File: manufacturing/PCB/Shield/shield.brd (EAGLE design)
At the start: 95 x 85 mm, 230 parts, among them J1 DC_JACK, Q1 12 MHz, T1 PHKD3NQ10T, U1 UCC27531, U10 UCC27531, U11 UCC27531, U12 UCC27531, U13 UCC27531, U14 UCC27531, U15 UCC27531, U16 UCC27531, U17 UCC27531, U18 UCC27531, U19 UCC27531, U2 UCC27531, U20 UCC27531, U21 UCC27531, U22 UCC27531, U23 UCC27531, U24 UCC27531, U25 UCC27531, U26 UCC27531, U27 UCC27531, U28 UCC27531, U29 UCC27531, U3 UCC27531, U30 UCC27531, U31 UCC27531, U32 UCC27531, U33 UCC27531, U34 UCC27531, U35 UCC27531, U36 UCC27531, U37 UCC27531, U38 UCC27531, U39 UCC27531, U4 UCC27531, U40 UCC27531, U41 UCC27531, U42 UCC27531, U43 UCC27531, U44 UCC27531, U45 UCC27531, U46 UCC27531, U47 UCC27531, U48 UCC27531, U49 UCC27531, U5 UCC27531, U50 UCC27531, U51 UCC27531, U52 UCC27531, U53 UCC27531, U54 UCC27531, U55 UCC27531, U56 UCC27531, U57 UCC27531, U58 UCC27531, U59 UCC27531, U6 UCC27531, U60 UCC27531, U61 UCC27531, U62 UCC27531, U63 UCC27531, U64 UCC27531, U65 LTC4365, U66 FT232R, U7 UCC27531, U8 UCC27531, U9 UCC27531, X1 MINI-USB, X2 BNC

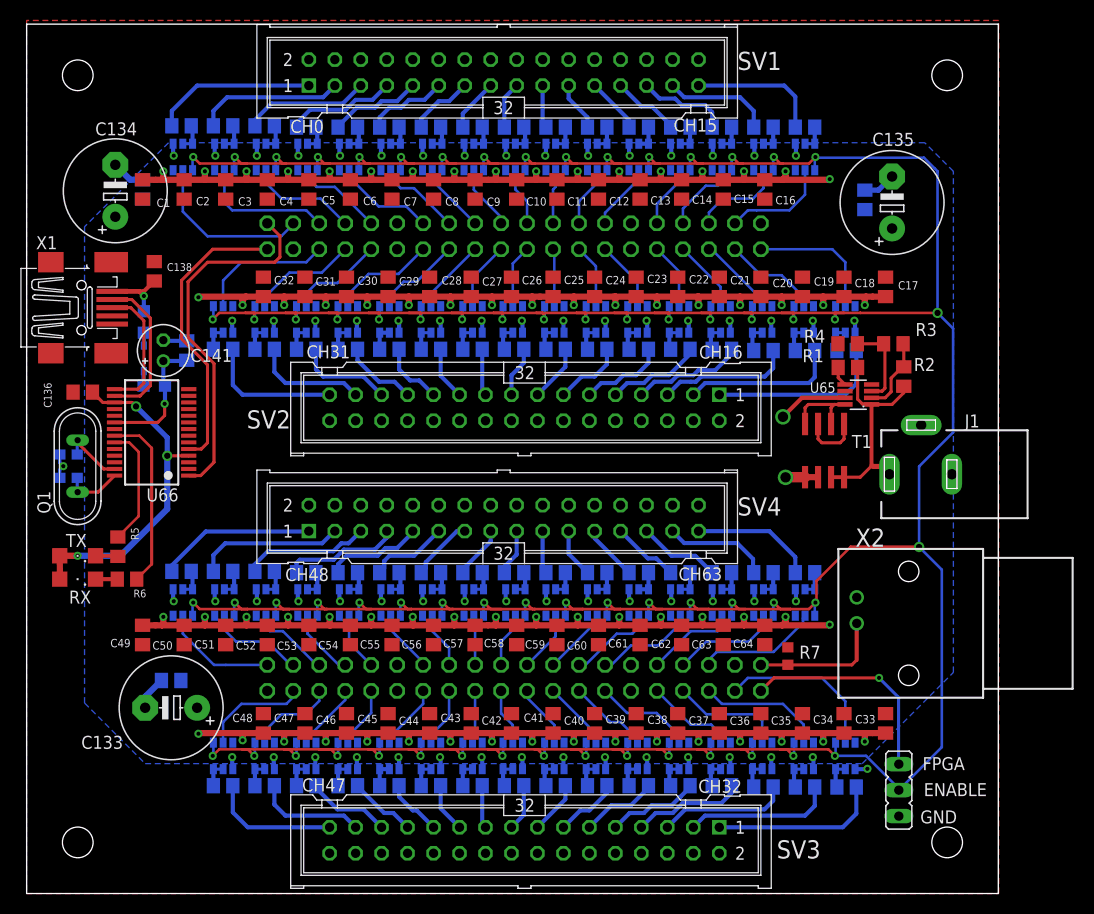
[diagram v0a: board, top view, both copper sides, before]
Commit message: fixed RX/TX swap, added power from USB option (Shield v1.1 ready for production)
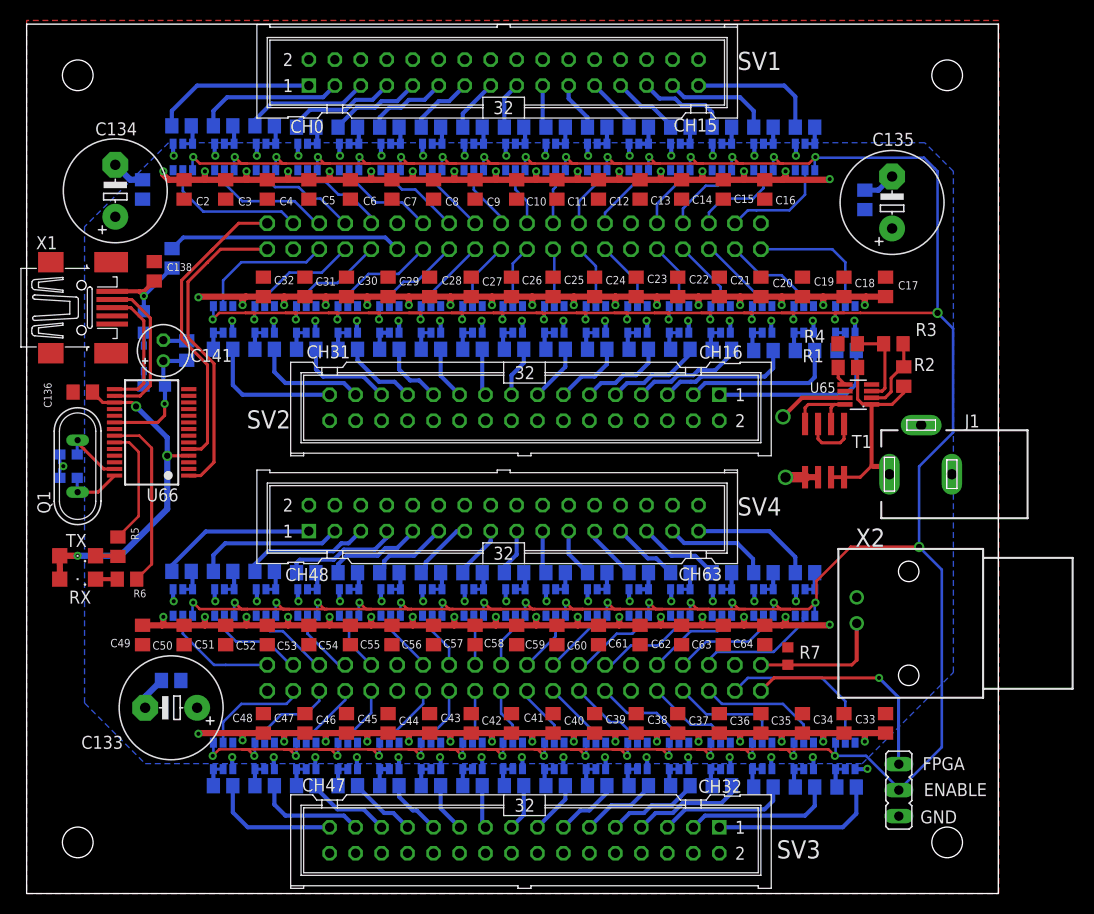
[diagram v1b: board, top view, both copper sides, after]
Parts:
- removed C1: 1uF, eagle-ltspice:C0805
- added R8: 0R, rcl:R0805
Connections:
- new net N$1: JP1.12, R8.2
- net GND: no longer C1.2
- net RX: now also JP1.1; no longer JP1.2
- net TX: now also JP1.2; no longer JP1.1
- net VBUS: now also R8.1
- net VDD: no longer C1.1
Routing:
- net N$1: track 0.00 -> 22.9 mm
- net TX: track 35.5 -> 30.8 mm
- net VDD: track 332.5 -> 330.0 mm
- net VBUS: track 8.11 -> 10.6 mm
- net IN0: track 16.4 -> 14.1 mm
- net IN1: track 13.3 -> 12.2 mm
- net RX: track 28.7 -> 29.7 mm
